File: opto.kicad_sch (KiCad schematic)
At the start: 18 parts, among them J5 UART_Device, U1 SN74LVC1G17DBVR, U10 TLP2361(TPL,E(T, U5 SN74LVC1G17DBVR, U8 SN74LVC1G17DBVR, U9 TLP2361(TPL,E(T

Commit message: Fix tlp2631 symbol recommended footprint from Package_SO:SO-6 to Package_SO:SO-5
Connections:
- net at U10.3: now also R23.1

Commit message: Switch footprints to stock KiCad versions, if the stock one is equivalent
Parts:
- U1, U5, U8: footprint pypilot_footprints:SOT-23-5 -> Package_TO_SOT_SMD:SOT-23-5
- U10, U9: footprint pypilot_footprints:SO-5_4.4x3.6mm_P1.27mm -> Package_SO:SO-5_4.4x3.6mm_P1.27mm
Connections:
- net at U10.3: now also R23.1
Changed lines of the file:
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@@
 	)
 	(symbol
+		(lib_name "pypilot_components:tlp2361")
 		(lib_id "pypilot_components:tlp2361")
 		(at 182.88 40.64 0)
@@
 			)
 		)
-		(property "Footprint" "pypilot_footprints:SO-5_4.4x3.6mm_P1.27mm"
+		(property "Footprint" "Package_SO:SO-5_4.4x3.6mm_P1.27mm"
 			(at 180.594 40.64 0)
 			(effects
@@
 		(pin "6"
 		)
+		(instances
+			(project "pypilot_controller"
+				(path "/3485d22d-0932-4f13-a5db-09c3f9bc7038/00000000-0000-0000-0000-000059d8755c/00000000-0000-0000-0000-0000664cd974"
+					(reference "U10")
+					(unit 1)
+				)
+			)
+		)
 	)
 	(symbol
@@
 			)
 		)
-		(property "Footprint" "pypilot_footprints:SOT-23-5"
+		(property "Footprint" "Package_TO_SOT_SMD:SOT-23-5"
 			(at 137.16 43.18 0)
 			(effects
@@
 			)
 		)
-		(property "Footprint" "pypilot_footprints:SO-5_4.4x3.6mm_P1.27mm"
+		(property "Footprint" "Package_SO:SO-5_4.4x3.6mm_P1.27mm"
 			(at 175.006 54.61 0)
 			(effects
@@
 		)
 		(pin "6"
+		)
+		(instances
+			(project "pypilot_controller"
+				(path "/3485d22d-0932-4f13-a5db-09c3f9bc7038/00000000-0000-0000-0000-000059d8755c/00000000-0000-0000-0000-0000664cd974"
+					(reference "U9")
+					(unit 1)
+				)
+			)
 		)
 	)
@@
 			)
 		)
-		(property "Footprint" "pypilot_footprints:SOT-23-5"
+		(property "Footprint" "Package_TO_SOT_SMD:SOT-23-5"
 			(at 115.57 54.61 0)
 			(effects
@@
 			)
 		)
-		(property "Footprint" "pypilot_footprints:SOT-23-5"
+		(property "Footprint" "Package_TO_SOT_SMD:SOT-23-5"
 			(at 134.62 50.8 0)
 			(effects

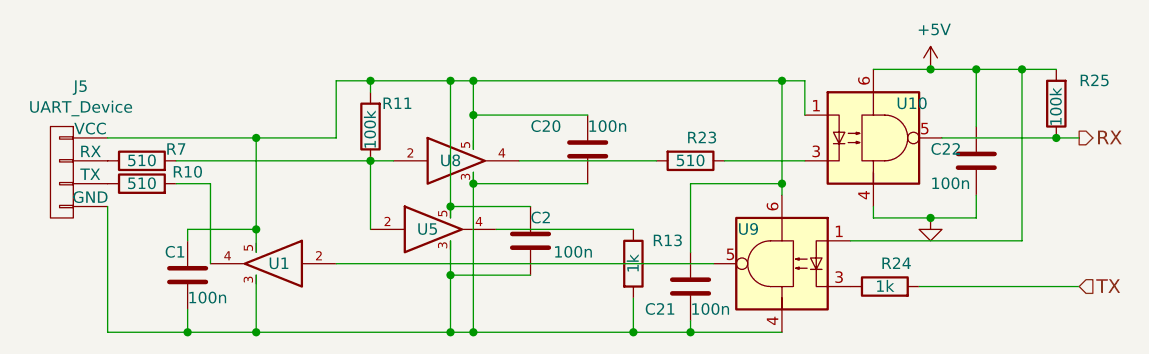
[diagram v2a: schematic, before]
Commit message: Adjusted power pins on 74AHC1G125
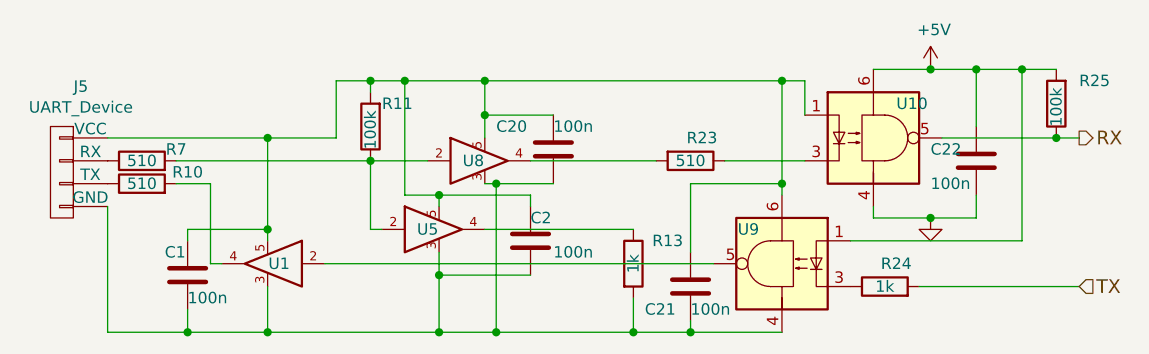
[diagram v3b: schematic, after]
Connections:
- net at U10.3: now also R23.1
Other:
- moved on the sheet: C20, U8

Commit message: Use stock KiCad symbols instead of Freetronics ones.
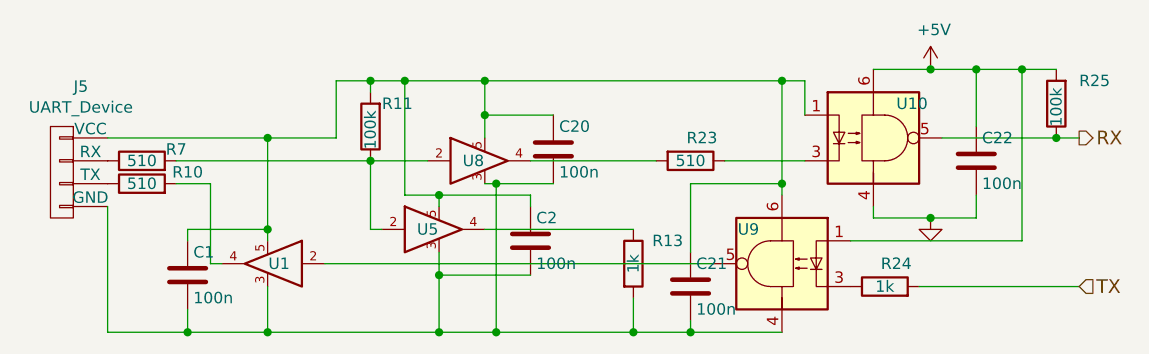
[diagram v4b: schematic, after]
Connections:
- net at U10.3: now also R23.1
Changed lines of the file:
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@@
 		(dnp no)
 		(property "Reference" "C22"
-			(at 189.23 41.91 0)
+			(at 194.945 40.64 0)
 			(effects
 				(font
@@
 		)
 		(property "Value" "100n"
-			(at 189.23 45.72 0)
+			(at 194.945 45.72 0)
 			(effects
 				(font
@@
 			)
 		)
-		(property "Description" ""
+		(property "Description" "Unpolarized capacitor"
 			(at 194.31 43.18 0)
 			(effects
@@
 		(pin "2"
 		)
+		(instances
+			(project "pypilot_controller"
+				(path "/3485d22d-0932-4f13-a5db-09c3f9bc7038/00000000-0000-0000-0000-000059d8755c/00000000-0000-0000-0000-0000664cd974"
+					(reference "C22")
+					(unit 1)
+				)
+			)
+		)
 	)
 	(symbol
@@
 		(dnp no)
 		(property "Reference" "C21"
-			(at 157.48 59.69 0)
+			(at 163.195 54.61 0)
 			(effects
 				(font
@@
 		)
 		(property "Value" "100n"
-			(at 162.56 59.69 0)
+			(at 163.195 59.69 0)
 			(effects
 				(font
@@
 			)
 		)
-		(property "Description" ""
+		(property "Description" "Unpolarized capacitor"
 			(at 162.56 57.15 0)
 			(effects
@@
 		)
 		(pin "2"
+		)
+		(instances
+			(project "pypilot_controller"
+				(path "/3485d22d-0932-4f13-a5db-09c3f9bc7038/00000000-0000-0000-0000-000059d8755c/00000000-0000-0000-0000-0000664cd974"
+					(reference "C21")
+					(unit 1)
+				)
+			)
 		)
 	)
@@
 		(dnp no)
 		(property "Reference" "C1"
-			(at 104.14 53.34 0)
+			(at 107.315 53.34 0)
 			(effects
 				(font
@@
 		)
 		(property "Value" "100n"
-			(at 106.68 58.42 0)
+			(at 107.315 58.42 0)
 			(effects
 				(font
@@
 			)
 		)
-		(property "Description" ""
+		(property "Description" "Unpolarized capacitor"
 			(at 106.68 55.88 0)
 			(effects
@@
 		(pin "2"
 		)
+		(instances
+			(project "pypilot_controller"
+				(path "/3485d22d-0932-4f13-a5db-09c3f9bc7038/00000000-0000-0000-0000-000059d8755c/00000000-0000-0000-0000-0000664cd974"
+					(reference "C1")
+					(unit 1)
+				)
+			)
+		)
 	)
 	(symbol
@@
 		(dnp no)
 		(property "Reference" "C2"
-			(at 144.78 49.53 0)
+			(at 145.415 49.53 0)
 			(effects
 				(font
@@
 		)
 		(property "Value" "100n"
-			(at 147.32 53.34 0)
+			(at 145.415 54.61 0)
 			(effects
 				(font
@@
 			)
 		)
-		(property "Description" ""
+		(property "Description" "Unpolarized capacitor"
 			(at 144.78 52.07 0)
 			(effects
@@
 		(pin "2"
 		)
+		(instances
+			(project "pypilot_controller"
+				(path "/3485d22d-0932-4f13-a5db-09c3f9bc7038/00000000-0000-0000-0000-000059d8755c/00000000-0000-0000-0000-0000664cd974"
+					(reference "C2")
+					(unit 1)
+				)
+			)
+		)
 	)
 	(symbol
@@
 		(dnp no)
 		(property "Reference" "C20"
-			(at 140.97 39.37 0)
+			(at 147.955 39.37 0)
 			(effects
 				(font
@@
 		)
 		(property "Value" "100n"
-			(at 147.32 39.37 0)
+			(at 147.955 44.45 0)
 			(effects
 				(font
@@
 			)
 		)
-		(property "Description" ""
+		(property "Description" "Unpolarized capacitor"
 			(at 147.32 41.91 0)
 			(effects
@@
 		(pin "2"
 		)
-	)
+		(instances
+			(project "pypilot_controller"
+				(path "/3485d22d-0932-4f13-a5db-09c3f9bc7038/00000000-0000-0000-0000-000059d8755c/00000000-0000-0000-0000-0000664cd974"
+					(reference "C20")
+					(unit 1)
+				)
+			)
+		)
+	)

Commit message: Move the UART header symbol from the uart sym lib to pypilot_components sym lib
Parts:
- J5: symbol uart:UART_Device -> pypilot_components:UART_Device
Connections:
- net at U10.3: now also R23.1
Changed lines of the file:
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@@
 	)
 	(symbol
-		(lib_id "uart:UART_Device")
+		(lib_id "pypilot_components:UART_Device")
 		(at 92.71 43.18 0)
 		(mirror y)

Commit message: Replace 74AHC1G125 with 74LVC1G17
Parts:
- U1, U5, U8: symbol pypilot_components:74AHC1G125 -> pypilot_components:74LVC1G17
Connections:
- net at U10.3: now also R23.1
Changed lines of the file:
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@@
+	(wire
+		(pts
+			(xy 139.7 50.8) (xy 156.21 50.8)
+		)
+		(stroke
+			(width 0)
+			(type default)
+		)
+	)
 	(wire
 		(pts
@@
 		(pts
 			(xy 140.97 62.23) (xy 156.21 62.23)
-		)
-		(stroke
-			(width 0)
-			(type default)
-		)
-	)
-	(wire
-		(pts
-			(xy 139.7 50.8) (xy 156.21 50.8)
 		)
 		(stroke
@@
 	)
 	(symbol
-		(lib_id "pypilot_components:74AHC1G125")
+		(lib_id "pypilot_components:74LVC1G17")
 		(at 139.7 43.18 0)
 		(unit 1)
@@
 	)
 	(symbol
-		(lib_id "pypilot_components:74AHC1G125")
+		(lib_id "pypilot_components:74LVC1G17")
 		(at 115.57 54.61 0)
 		(mirror y)
@@
 	)
 	(symbol
-		(lib_id "pypilot_components:74AHC1G125")
+		(lib_id "pypilot_components:74LVC1G17")
 		(at 134.62 50.8 0)
 		(unit 1)

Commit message: Add missing designators to schematic
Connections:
- net at U10.3: now also R23.1
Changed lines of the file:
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@@
 		(pin "4"
+		)
+		(instances
+			(project "pypilot_controller"
+				(path "/3485d22d-0932-4f13-a5db-09c3f9bc7038/00000000-0000-0000-0000-000059d8755c/00000000-0000-0000-0000-0000664cd974"
+					(reference "J5")
+					(unit 1)
+				)
+			)
 		)
 	)
@@
 		(pin "2"
 		)
+		(instances
+			(project "pypilot_controller"
+				(path "/3485d22d-0932-4f13-a5db-09c3f9bc7038/00000000-0000-0000-0000-000059d8755c/00000000-0000-0000-0000-0000664cd974"
+					(reference "R25")
+					(unit 1)
+				)
+			)
+		)
 	)
 	(symbol
@@
 		(pin "2"
 		)
+		(instances
+			(project "pypilot_controller"
+				(path "/3485d22d-0932-4f13-a5db-09c3f9bc7038/00000000-0000-0000-0000-000059d8755c/00000000-0000-0000-0000-0000664cd974"
+					(reference "R10")
+					(unit 1)
+				)
+			)
+		)
 	)
 	(symbol
@@
 		(pin "5"
 		)
+		(instances
+			(project "pypilot_controller"
+				(path "/3485d22d-0932-4f13-a5db-09c3f9bc7038/00000000-0000-0000-0000-000059d8755c/00000000-0000-0000-0000-0000664cd974"
+					(reference "U8")
+					(unit 1)
+				)
+			)
+		)
 	)
 	(symbol
@@
 		(pin "2"
 		)
+		(instances
+			(project "pypilot_controller"
+				(path "/3485d22d-0932-4f13-a5db-09c3f9bc7038/00000000-0000-0000-0000-000059d8755c/00000000-0000-0000-0000-0000664cd974"
+					(reference "R11")
+					(unit 1)
+				)
+			)
+		)
 	)
 	(symbol
@@
 		(pin "2"
 		)
+		(instances
+			(project "pypilot_controller"
+				(path "/3485d22d-0932-4f13-a5db-09c3f9bc7038/00000000-0000-0000-0000-000059d8755c/00000000-0000-0000-0000-0000664cd974"
+					(reference "R23")
+					(unit 1)
+				)
+			)
+		)
 	)
 	(symbol
@@
 		)
 		(pin "2"
+		)
+		(instances
+			(project "pypilot_controller"
+				(path "/3485d22d-0932-4f13-a5db-09c3f9bc7038/00000000-0000-0000-0000-000059d8755c/00000000-0000-0000-0000-0000664cd974"
+					(reference "R24")
+					(unit 1)
+				)
+			)
 		)
 	)
@@
 		(pin "5"
 		)
+		(instances
+			(project "pypilot_controller"
+				(path "/3485d22d-0932-4f13-a5db-09c3f9bc7038/00000000-0000-0000-0000-000059d8755c/00000000-0000-0000-0000-0000664cd974"
+					(reference "U1")
+					(unit 1)
+				)
+			)
+		)
 	)
 	(symbol
@@
 		(pin "5"
 		)
+		(instances
+			(project "pypilot_controller"
+				(path "/3485d22d-0932-4f13-a5db-09c3f9bc7038/00000000-0000-0000-0000-000059d8755c/00000000-0000-0000-0000-0000664cd974"
+					(reference "U5")
+					(unit 1)
+				)
+			)
+		)
 	)
 	(symbol
@@
 		(pin "2"
 		)
+		(instances
+			(project "pypilot_controller"
+				(path "/3485d22d-0932-4f13-a5db-09c3f9bc7038/00000000-0000-0000-0000-000059d8755c/00000000-0000-0000-0000-0000664cd974"
+					(reference "R13")
+					(unit 1)
+				)
+			)
+		)
 	)
 	(symbol
@@
 		(pin "2"
 		)
-	)
+		(instances
+			(project "pypilot_controller"
+				(path "/3485d22d-0932-4f13-a5db-09c3f9bc7038/00000000-0000-0000-0000-000059d8755c/00000000-0000-0000-0000-0000664cd974"
+					(reference "R7")
+					(unit 1)
+				)
+			)
+		)
+	)

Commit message: Update every symbol in the schematic
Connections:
- net at U10.3: now also R23.1
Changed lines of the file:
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@@
 		)
 		(property "Footprint" "Resistor_SMD:R_0805_2012Metric"
-			(at 206.121 36.83 90)
+			(at 204.978 36.83 90)
 			(effects
 				(font
@@
 			)
 		)
-		(property "Description" ""
+		(property "Description" "Resistor"
 			(at 203.2 36.83 0)
 			(effects
@@
 		)
 		(property "Footprint" "Resistor_SMD:R_0805_2012Metric"
-			(at 101.6 48.641 90)
+			(at 101.6 47.498 90)
 			(effects
 				(font
@@
 			)
 		)
-		(property "Description" ""
+		(property "Description" "Resistor"
 			(at 101.6 45.72 0)
 			(effects
@@
 		)
 		(property "Footprint" "Resistor_SMD:R_0805_2012Metric"
-			(at 129.921 39.37 90)
+			(at 128.778 39.37 90)
 			(effects
 				(font
@@
 			)
 		)
-		(property "Description" ""
+		(property "Description" "Resistor"
 			(at 127 39.37 0)
 			(effects
@@
 		)
 		(property "Footprint" "Resistor_SMD:R_0805_2012Metric"
-			(at 162.56 40.259 90)
+			(at 162.56 41.402 90)
 			(effects
 				(font
@@
 			)
 		)
-		(property "Description" ""
+		(property "Description" "Resistor"
 			(at 162.56 43.18 0)
 			(effects
@@
 		)
 		(property "Footprint" "Resistor_SMD:R_0805_2012Metric"
-			(at 184.15 60.071 90)
+			(at 184.15 58.928 90)
 			(effects
 				(font
@@
 			)
 		)
-		(property "Description" ""
+		(property "Description" "Resistor"
 			(at 184.15 57.15 0)
 			(effects
@@
 	)
 	(symbol
+		(lib_name "pypilot_components:tlp2361")
 		(lib_id "pypilot_components:tlp2361")
 		(at 172.72 54.61 0)
@@
 		)
 		(property "Footprint" "Resistor_SMD:R_0805_2012Metric"
-			(at 153.289 54.61 90)
+			(at 154.432 54.61 90)
 			(effects
 				(font
@@
 			)
 		)
-		(property "Description" ""
+		(property "Description" "Resistor"
 			(at 156.21 54.61 0)
 			(effects
@@
 			)
 		)
-		(property "Description" ""
+		(property "Description" "Power symbol creates a global label with name \"GND\" , ground"
 			(at 189.23 49.53 0)
 			(effects
@@
 			)
 		)
-		(property "Description" ""
+		(property "Description" "Power symbol creates a global label with name \"+5V\""
 			(at 189.23 33.02 0)
 			(effects
@@
 		)
 		(property "Footprint" "Resistor_SMD:R_0805_2012Metric"
-			(at 101.6 46.101 90)
+			(at 101.6 44.958 90)
 			(effects
 				(font
@@
 			)
 		)
-		(property "Description" ""
+		(property "Description" "Resistor"
 			(at 101.6 43.18 0)
 			(effects
